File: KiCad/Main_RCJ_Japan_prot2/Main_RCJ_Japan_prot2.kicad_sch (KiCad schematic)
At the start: 13 parts, among them J1 Conn_01x04_Socket, J2 Conn_01x04_Socket, J3 Conn_01x04_Socket, J4 Conn_01x04_Socket, J5 Conn_01x04_Socket, J6 Conn_01x04_Socket

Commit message: あ
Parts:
- added BZ1: Buzzer, symbol Device:Buzzer
- D1: footprint (none) -> Capacitor_SMD:C_0603_1608Metric_Pad1.08x0.95mm_HandSolder
- H1, H2, H3, H4: footprint (none) -> MountingHole:MountingHole_3.2mm_M3
- J1, J2, J3, J4, J5, J6: footprint (none) -> Connector_JST:JST_PH_B4B-PH-K_1x04_P2.00mm_Vertical
- R1: footprint (none) -> Resistor_SMD:R_0603_1608Metric_Pad0.98x0.95mm_HandSolder
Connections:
- net GND: now reaches A1.13 (GND), A1.18 (GND), A1.23 (GND), A1.28 (GND), A1.3 (GND), A1.38 (GND), A1.8 (GND), A1.D2 (GND)
- net GND: now also A1.33 (AGND)
- net VCC: now reaches A1.39 (VSYS)
- net SDA: now reaches A1.6 (GPIO4)
- net SCL: now reaches A1.7 (GPIO5)
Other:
- note added: "5V"
- note added: "NC"
- note added: "PH"

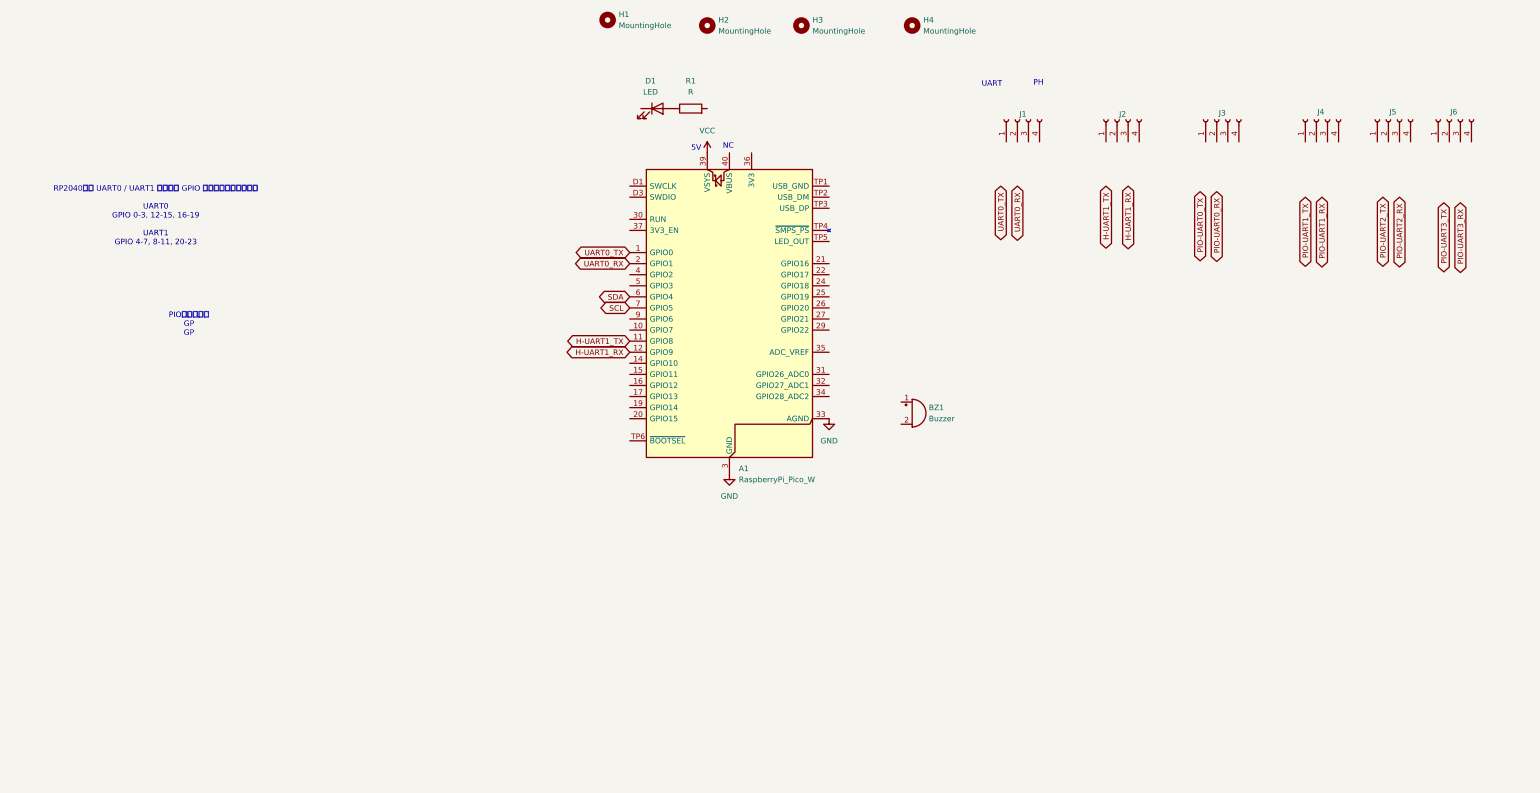
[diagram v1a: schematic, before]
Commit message: 新メイン仮配置完了
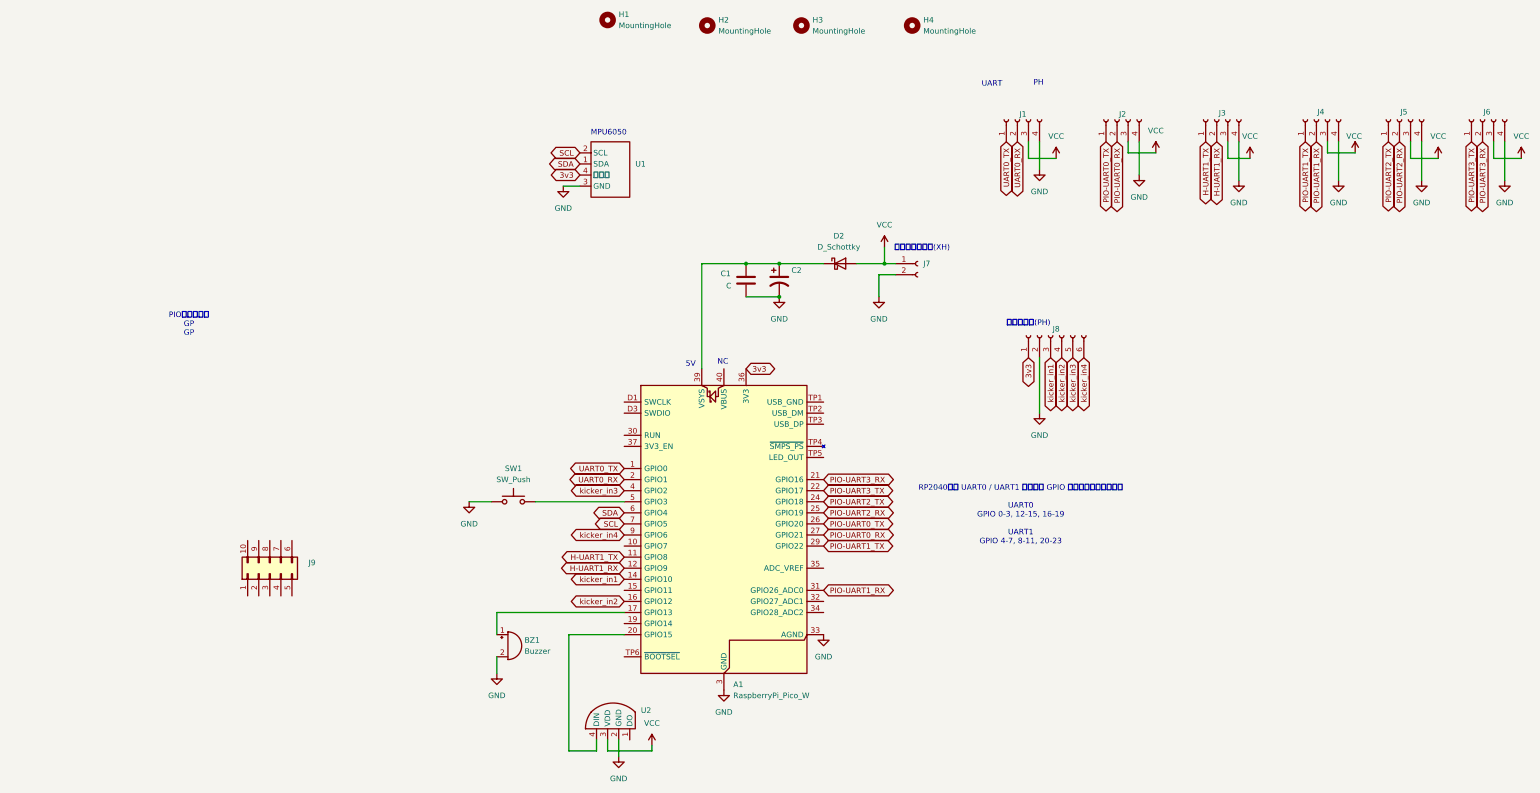
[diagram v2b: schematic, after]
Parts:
- removed D1: LED, Capacitor_SMD:C_0603_1608Metric_Pad1.08x0.95mm_HandSolder, symbol Device:LED
- removed R1: R, Resistor_SMD:R_0603_1608Metric_Pad0.98x0.95mm_HandSolder, symbol Device:R
- added C1: C, Capacitor_SMD:C_0603_1608Metric_Pad1.08x0.95mm_HandSolder, symbol Device:C
- added C2: C_Polarized_US, Capacitor_THT:CP_Radial_D8.0mm_P3.50mm, symbol Device:C_Polarized_US
- added D2: D_Schottky, Diode_SMD:D_SOD-123, symbol Device:D_Schottky
- added J7: Conn_01x02_Socket, Connector_JST:JST_XH_S2B-XH-A_1x02_P2.50mm_Horizontal, symbol Connector:Conn_01x02_Socket
- added J8: Conn_01x06_Socket, Connector_JST:JST_PH_S6B-PH-K_1x06_P2.00mm_Horizontal, symbol Connector:Conn_01x06_Socket
- added J9: Conn_02x05_Counter_Clockwise, symbol Connector_Generic:Conn_02x05_Counter_Clockwise
- added SW1: SW_Push, Button_Switch_THT:SW_PUSH_6mm, symbol Switch:SW_Push
- added U1: ~, MPU:名称未設定, symbol MPU6050:MPU
- added U2: ~, PL9823-F5(RGBLED):名称未設定, symbol PL9823-F5(RGBLED):PL9823-F5
- A1: footprint Module:RaspberryPi_Pico_W_SMD -> Module:RaspberryPi_Pico_Common_Unspecified
- BZ1: footprint (none) -> Buzzer_Beeper:Buzzer_12x9.5RM7.6
- J1, J2: footprint Connector_JST:JST_PH_B4B-PH-K_1x04_P2.00mm_Vertical -> Connector_JST:JST_PH_S4B-PH-K_1x04_P2.00mm_Horizontal
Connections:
- net GND: now also BZ1.2 (-), J1.4 (Pin_4), J2.4 (Pin_4), J3.4 (Pin_4), J4.4 (Pin_4), J5.4 (Pin_4), J6.4 (Pin_4), C1.2, C2.2, J7.2 (Pin_2), J8.2 (Pin_2), SW1.1, U1.3 (GND), U2.2 (GND)
- net H-UART1_RX: now also J3.2 (Pin_2)
- net H-UART1_TX: now also J3.1 (Pin_1)
- net PIO-UART0_RX: now also A1.27 (GPIO21), J2.2 (Pin_2)
- net PIO-UART0_TX: now also A1.26 (GPIO20), J2.1 (Pin_1)
- net PIO-UART1_RX: now also A1.31 (GPIO26_ADC0), J4.2 (Pin_2)
- net PIO-UART1_TX: now also A1.29 (GPIO22), J4.1 (Pin_1)
- net PIO-UART2_RX: now also A1.25 (GPIO19), J5.2 (Pin_2)
- net PIO-UART2_TX: now also A1.24 (GPIO18), J5.1 (Pin_1)
- net PIO-UART3_RX: now also A1.21 (GPIO16), J6.2 (Pin_2)
- net PIO-UART3_TX: now also A1.22 (GPIO17), J6.1 (Pin_1)
- net SCL: now also U1.2 (SCL)
- net SDA: now also U1.1 (SDA)
- net UART0_RX: now also J1.2 (Pin_2)
- net UART0_TX: now also J1.1 (Pin_1)
- net VCC: now also J1.3 (Pin_3), J2.3 (Pin_3), J3.3 (Pin_3), J4.3 (Pin_3), J5.3 (Pin_3), J6.3 (Pin_3), D2.2 (A), J7.1 (Pin_1), U2.3 (VDD); no longer A1.39 (VSYS)
- net kicker_in1: now reaches A1.14 (GPIO10)
- net kicker_in1: now also J8.3 (Pin_3)
- net kicker_in2: now reaches A1.16 (GPIO12)
- net kicker_in2: now also J8.4 (Pin_4)
- net at A1.17 (GPIO13): now also BZ1.1 (+)
- net at A1.20 (GPIO15): now also U2.4 (DIN)
- net 3v3: now reaches A1.36 (3V3)
- net 3v3: now also J8.1 (Pin_1), U1.4 (３ｖ３)
- net kicker_in3: now reaches A1.4 (GPIO2)
- net kicker_in3: now also J8.5 (Pin_5)
- net at A1.5 (GPIO3): now also SW1.2
- net kicker_in4: now reaches A1.9 (GPIO6)
- net kicker_in4: now also J8.6 (Pin_6)
- new net: A1.39 (VSYS), C1.1, C2.1, D2.1 (K)
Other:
- note added: "MPU6050"
- note added: "キッカー用(PH)"
- note added: "メイン電源入力(XH)"
- moved on the sheet: A1, BZ1, J5, J6

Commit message: 新メイン完成
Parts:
- removed J9: Conn_02x05_Counter_Clockwise, symbol Connector_Generic:Conn_02x05_Counter_Clockwise
- added C3: C, Capacitor_SMD:C_0603_1608Metric_Pad1.08x0.95mm_HandSolder, symbol Device:C
- added J10: Conn_01x02_Socket, Connector_JST:JST_XH_S2B-XH-A_1x02_P2.50mm_Horizontal, symbol Connector:Conn_01x02_Socket
- added J11, J12: Conn_01x03_Socket, Connector_JST:JST_PH_B3B-PH-K_1x03_P2.00mm_Vertical, symbol Connector:Conn_01x03_Socket
- added J13, J14: Conn_01x02_Socket, Connector_JST:JST_PH_B2B-PH-K_1x02_P2.00mm_Vertical, symbol Connector:Conn_01x02_Socket
- added J9: Conn_02x03_Odd_Even, Connector_PinHeader_2.54mm:PinHeader_2x03_P2.54mm_Vertical, symbol Connector_Generic:Conn_02x03_Odd_Even
- added R1, R2: R, Resistor_THT:R_Axial_DIN0309_L9.0mm_D3.2mm_P12.70mm_Horizontal, symbol Device:R
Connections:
- net 3v3: now also C3.1, J11.3 (Pin_3), J12.3 (Pin_3), J13.2 (Pin_2), J14.2 (Pin_2), J9.2 (Pin_2)
- net GND: now also C3.2, J10.2 (Pin_2), J11.2 (Pin_2), J12.2 (Pin_2), J13.1 (Pin_1), J14.1 (Pin_1), J9.3 (Pin_3), J9.4 (Pin_4)
- net PIO-UART1_RX: now also A1.15 (GPIO11); no longer A1.31 (GPIO26_ADC0)
- net VCC: no longer U2.3 (VDD)
- net at A1.39 (VSYS), C1.1, C2.1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: now also U2.3 (VDD), J9.1 (Pin_1)
- net at A1.10 (GPIO7): now also J9.6 (Pin_6)
- net at A1.19 (GPIO14): now also J9.5 (Pin_5)
- net ADC2: now reaches A1.32 (GPIO27_ADC1)
- net ADC2: now also J11.1 (Pin_1)
- net BATT_ADC: now reaches A1.34 (GPIO28_ADC2)
- net BATT_ADC: now also R1.2, R2.2
- new net: J10.1 (Pin_1), R1.1, R2.1
- new net ADC1: A1.31 (GPIO26_ADC0), J12.1 (Pin_1)
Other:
- note added: "3.3V供給(ph Holizonal)"
- note added: "ADC(ph Holizonal)"
- note added: "キッカー用(ph Holizonal)"
- note added: "バッテリー電圧測定ADC(XH Holizonal)"
- note removed: "キッカー用(PH)"
- moved on the sheet: J8

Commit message: 画像インポートクラッシュくそ
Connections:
- net GND: now also R2.1
- net at J10.1 (Pin_1), R1.1: no longer R2.1
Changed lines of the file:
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@@
-	)
-	(junction
-		(at 322.58 100.33)
-		(diameter 0)
-		(color 0 0 0 0)
 	)
 	(junction
@@
 	)
 	(junction
+		(at 325.12 109.22)
+		(diameter 0)
+		(color 0 0 0 0)
+	)
+	(junction
 		(at 87.63 80.01)
 		(diameter 0)
@@
 	(wire
 		(pts
+			(xy 322.58 109.22) (xy 325.12 109.22)
+		)
+		(stroke
+			(width 0)
+			(type default)
+		)
+	)
+	(wire
+		(pts
 			(xy 76.2 203.2) (xy 76.2 191.77)
 		)
@@
 	(wire
 		(pts
+			(xy 325.12 109.22) (xy 325.12 100.33)
+		)
+		(stroke
+			(width 0)
+			(type default)
+		)
+	)
+	(wire
+		(pts
 			(xy 132.08 80.01) (xy 129.54 80.01)
 		)
@@
 	(wire
 		(pts
-			(xy 322.58 100.33) (xy 322.58 109.22)
-		)
-		(stroke
-			(width 0)
-			(type default)
-		)
-	)
-	(wire
-		(pts
 			(xy 275.59 55.88) (xy 269.24 55.88)
 		)
@@
 	(wire
 		(pts
-			(xy 325.12 120.65) (xy 325.12 100.33)
-		)
-		(stroke
+			(xy 325.12 120.65) (xy 325.12 109.22)
+		)
+		(stroke
